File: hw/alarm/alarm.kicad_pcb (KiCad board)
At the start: 2 copper layers, 105 x 73 mm, 58 parts, among them IC1 DS3231S#T&R, IC2 TSOP38238, IC3 SHT40-BD1B-R2, IC4 23K256-I_SN, IC5 PEC11S-929K-S0015, J1 4328, J2 SFV24R-4STBE1HLF, Q1 DMG2305UX-7, Q3 Si1308EDL-T1-GE3, U1 RaspberryPi_Pico, U3 2462, U4 AS1115-BSST, U5 TDCR1060M

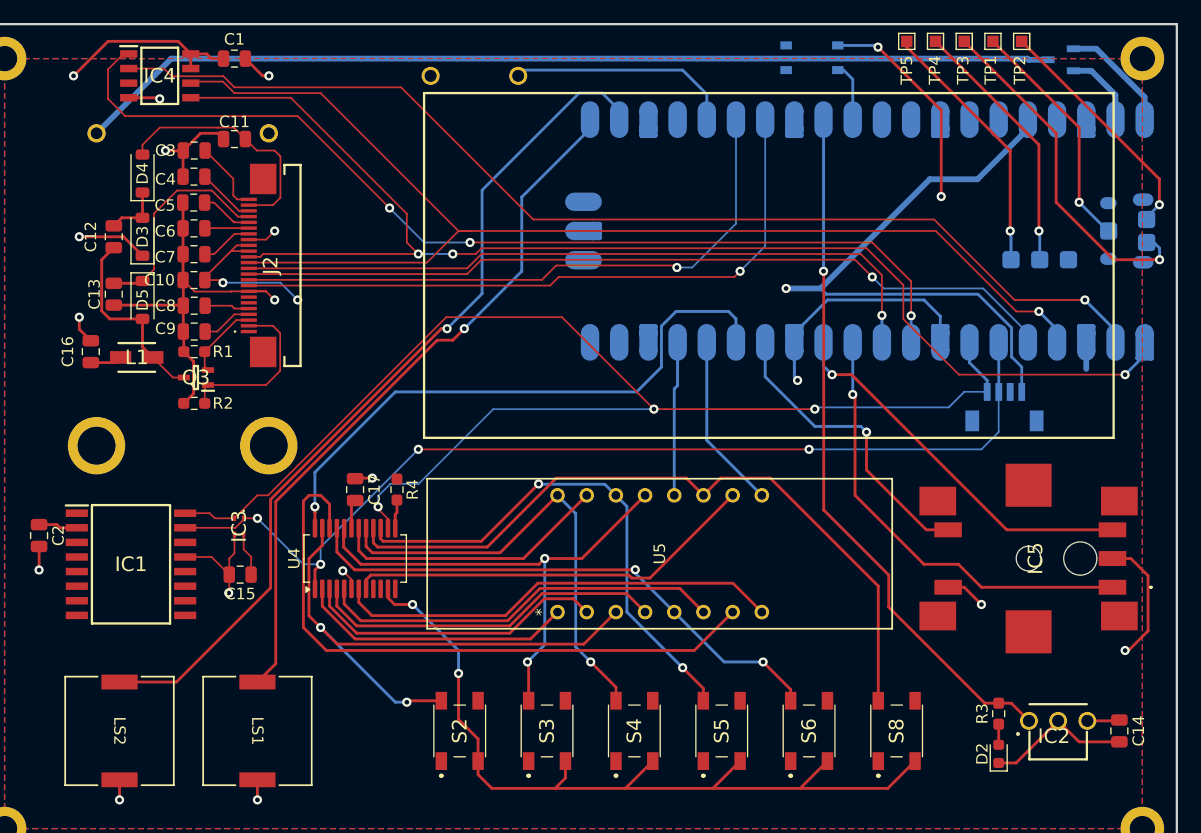
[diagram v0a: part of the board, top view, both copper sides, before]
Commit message: Make DRC-rec'd changes
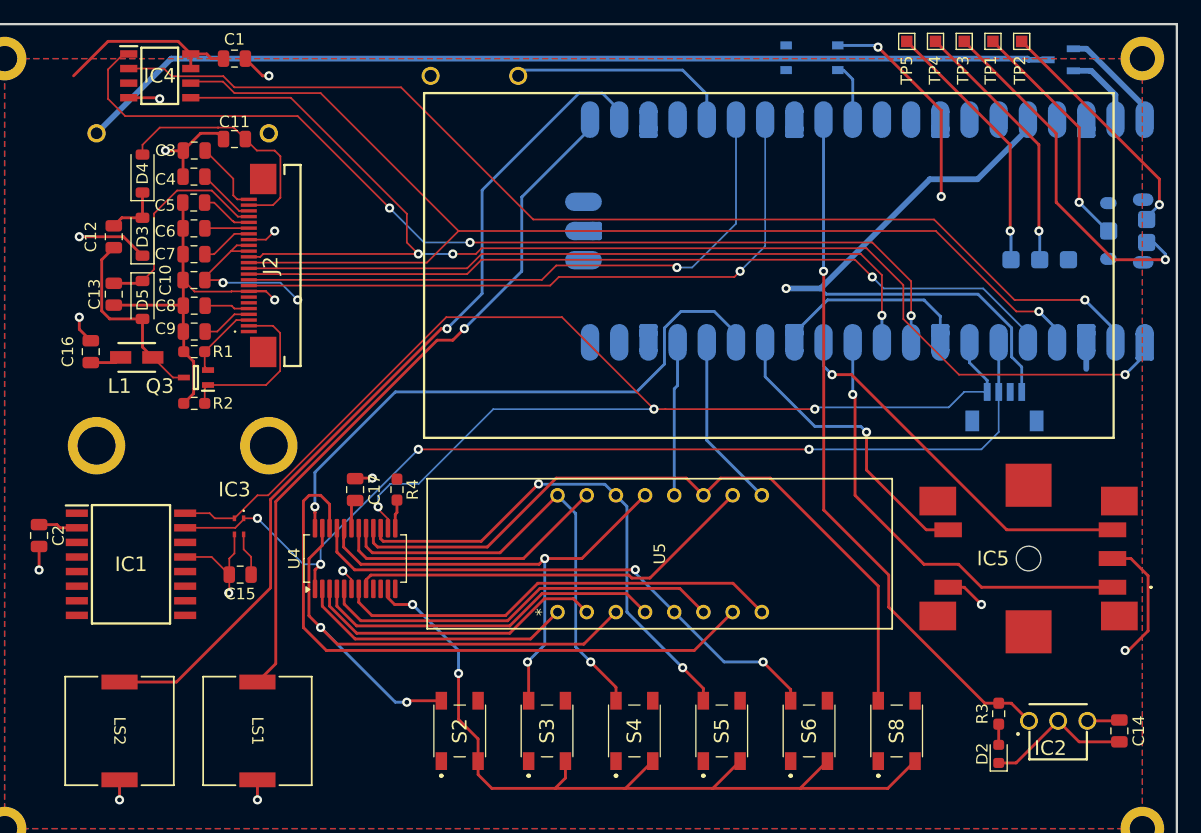
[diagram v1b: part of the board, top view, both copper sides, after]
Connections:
- J1 pad SH1: Net-(J1-SHIELD-PadSH1) -> unconnected-(J1-SHIELD-PadSH1)
- J1 pad SH2: Net-(J1-SHIELD-PadSH1) -> unconnected-(J1-SHIELD-PadSH2)
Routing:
- net GND: track 147.6 -> 143.4 mm, vias 18 -> 17
- net /SCK: track 105.1 -> 104.1 mm
- net /IRQ: track 50.9 -> 49.9 mm
- net Net-(U1-USB_DP): track 30.7 -> 31.4 mm
- net +3.3V: vias 4 -> 3

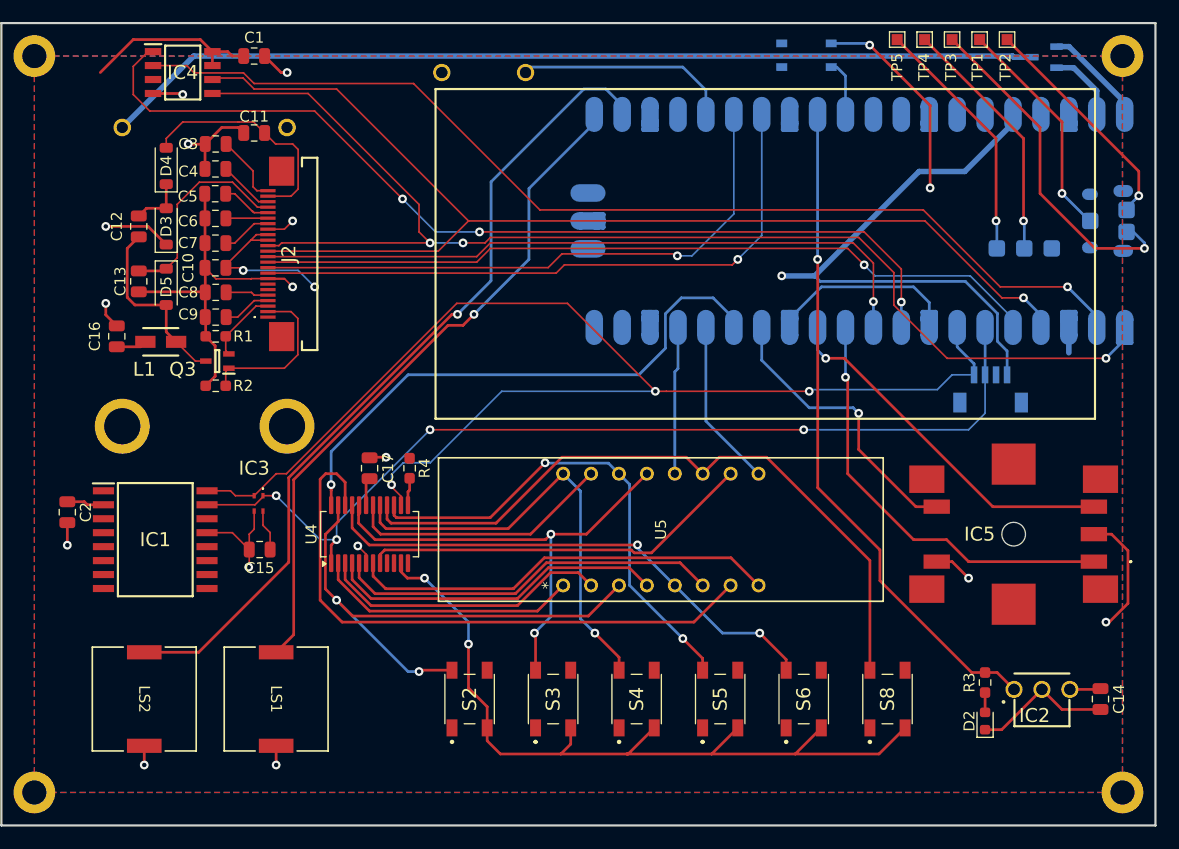
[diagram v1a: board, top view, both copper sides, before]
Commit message: Add pull-ups to i2c line, fix problems with DS3231 circuit
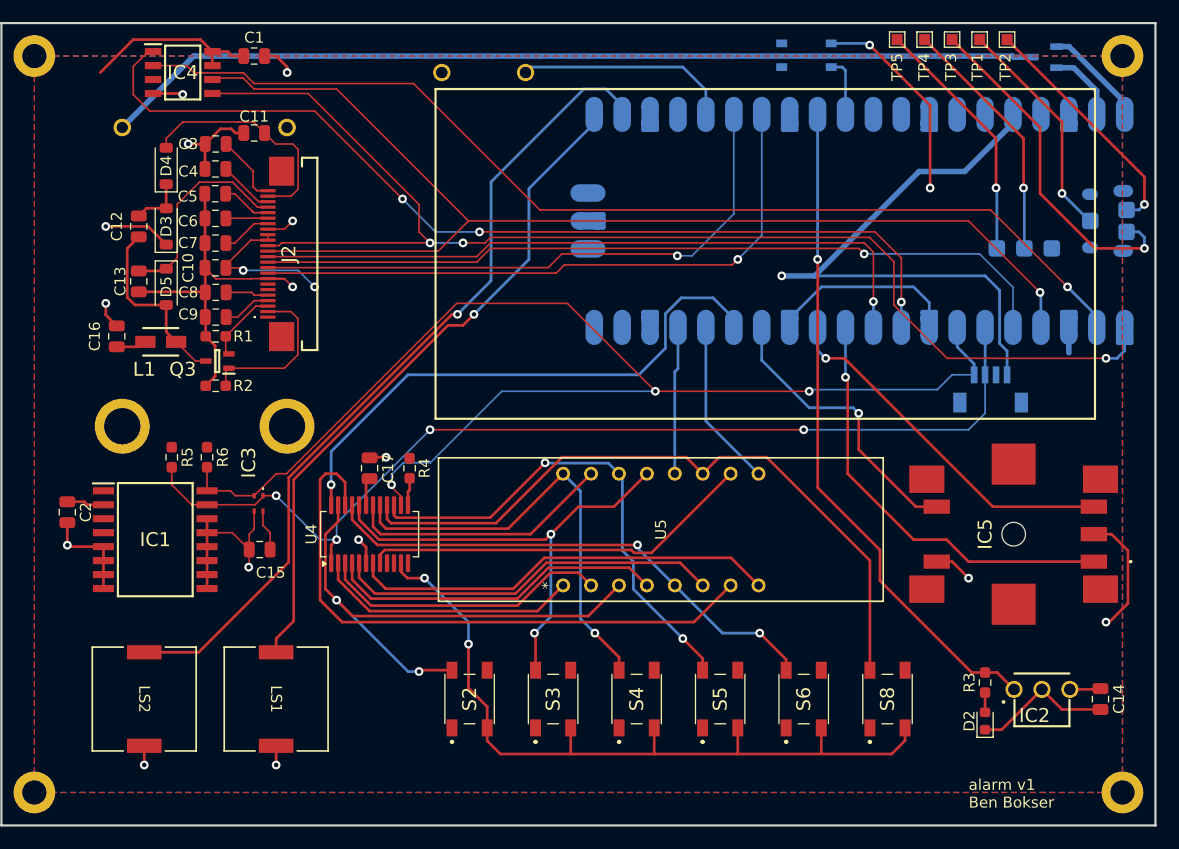
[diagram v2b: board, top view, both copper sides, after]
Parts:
- added R5: 10kΩ, Resistor_SMD:R_0603_1608Metric_Pad0.98x0.95mm_HandSolder, F.Cu at (104.0, 101.0)
- added R6: 10kΩ, Resistor_SMD:R_0603_1608Metric_Pad0.98x0.95mm_HandSolder, F.Cu at (107.2, 101.0)
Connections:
- IC1 pad 10: unconnected-(IC1-N.C._6-Pad10) -> GND
- IC1 pad 11: unconnected-(IC1-N.C._7-Pad11) -> GND
- IC1 pad 12: unconnected-(IC1-N.C._8-Pad12) -> GND
- IC1 pad 14: +3.3V -> GND
- IC1 pad 5: unconnected-(IC1-N.C._1-Pad5) -> GND
- IC1 pad 6: unconnected-(IC1-N.C._2-Pad6) -> GND
- IC1 pad 7: unconnected-(IC1-N.C._3-Pad7) -> GND
- IC1 pad 8: unconnected-(IC1-N.C._4-Pad8) -> GND
- IC1 pad 9: unconnected-(IC1-N.C._5-Pad9) -> GND
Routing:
- net GND: track 143.4 -> 157.6 mm
- net /SDA: track 89.4 -> 95.0 mm
- net /KEYA: track 72.8 -> 69.9 mm
- net /SCL: track 117.3 -> 119.4 mm
- net /DC: track 71.0 -> 72.6 mm
- net /SCK: track 104.1 -> 105.2 mm
- net /MOSI: track 114.1 -> 115.2 mm
- net Net-(U1-USB_DM): track 20.9 -> 22.0 mm
- net /SRAMCS: track 85.9 -> 86.5 mm
- net /EinkCS: track 61.4 -> 62.0 mm
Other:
- board text added: "alarm v1 Ben Bokser"
